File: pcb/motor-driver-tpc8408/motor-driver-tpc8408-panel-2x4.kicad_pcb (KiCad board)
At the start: 2 copper layers, 92 x 90 mm, 202 parts, among them J1 Conn_01x12, U1 TPC8408, U2 TPC8408, U3 74HC00

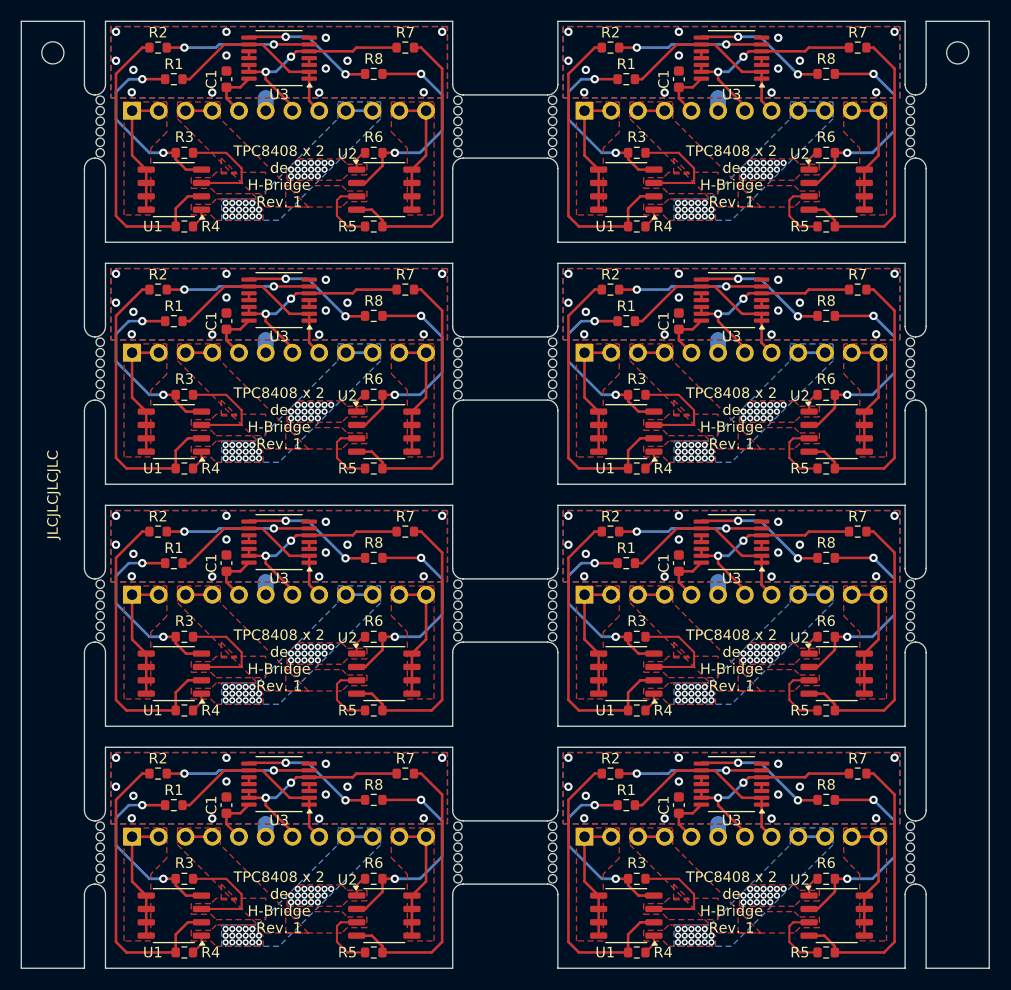
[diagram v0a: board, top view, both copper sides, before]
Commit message: 配線が間違っていたのを修正した
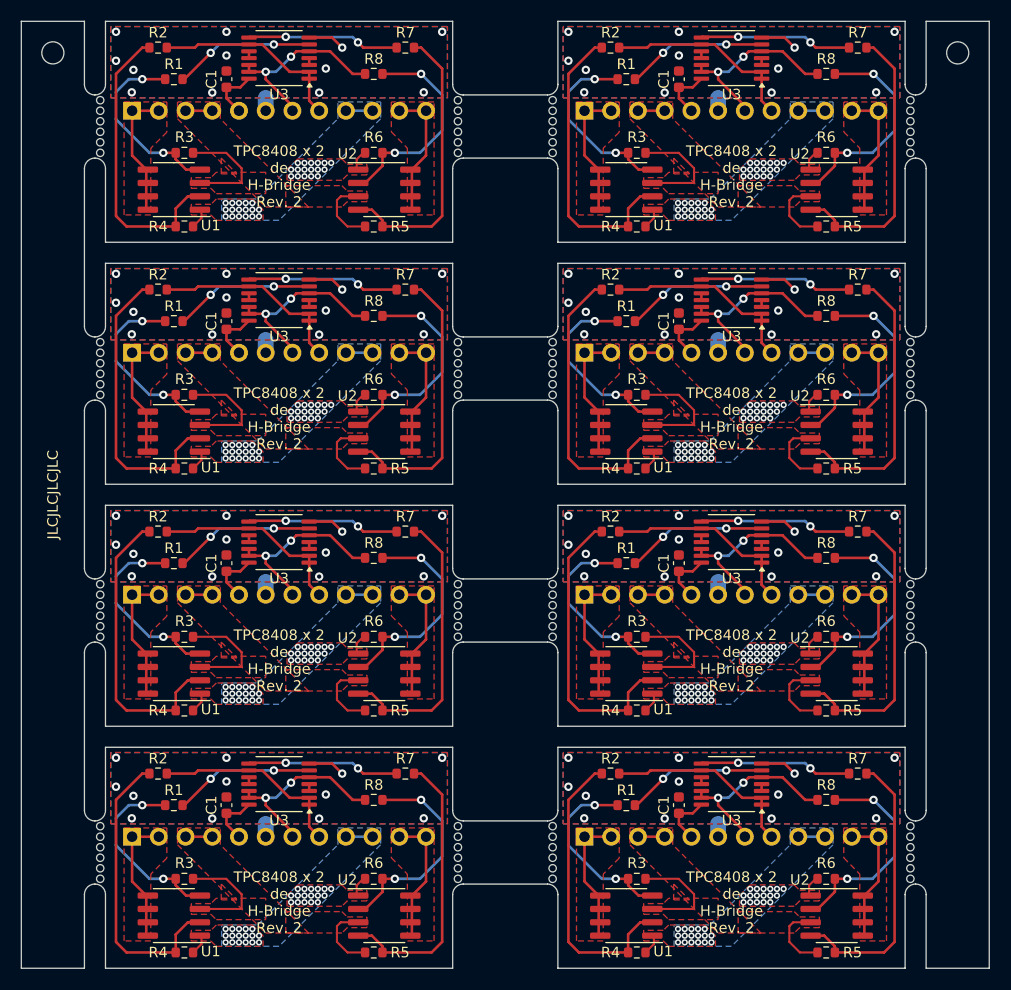
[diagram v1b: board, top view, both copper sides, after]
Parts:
- removed the U1 at (128.0, 115.0)
- removed the U1 at (128.0, 46.0)
- removed the U1 at (128.0, 69.0)
- removed the U1 at (171.0, 69.0)
- removed the U1 at (171.0, 46.0)
- removed the U1 at (171.0, 92.0)
- removed the U1 at (171.0, 115.0)
- removed the U1 at (128.0, 92.0)
- removed the U2 at (191.0, 69.0)
- removed the U2 at (191.0, 115.0)
- removed the U2 at (191.0, 92.0)
- removed the U2 at (148.0, 46.0)
- removed the U2 at (148.0, 115.0)
- removed the U2 at (148.0, 92.0)
- removed the U2 at (148.0, 69.0)
- removed the U2 at (191.0, 46.0)
- added U1: FDS4559, Package_SO:SOIC-8_3.9x4.9mm_P1.27mm, F.Cu at (128.0, 92.0)
- added U1: FDS4559, Package_SO:SOIC-8_3.9x4.9mm_P1.27mm, F.Cu at (171.0, 69.0)
- added U1: FDS4559, Package_SO:SOIC-8_3.9x4.9mm_P1.27mm, F.Cu at (171.0, 46.0)
- added U1: FDS4559, Package_SO:SOIC-8_3.9x4.9mm_P1.27mm, F.Cu at (128.0, 69.0)
- added U1: FDS4559, Package_SO:SOIC-8_3.9x4.9mm_P1.27mm, F.Cu at (128.0, 46.0)
- added U1: FDS4559, Package_SO:SOIC-8_3.9x4.9mm_P1.27mm, F.Cu at (128.0, 115.0)
- added U1: FDS4559, Package_SO:SOIC-8_3.9x4.9mm_P1.27mm, F.Cu at (171.0, 115.0)
- added U1: FDS4559, Package_SO:SOIC-8_3.9x4.9mm_P1.27mm, F.Cu at (171.0, 92.0)
- added U2: FDS4559, Package_SO:SOIC-8_3.9x4.9mm_P1.27mm, F.Cu at (148.0, 69.0)
- added U2: FDS4559, Package_SO:SOIC-8_3.9x4.9mm_P1.27mm, F.Cu at (191.0, 115.0)
- added U2: FDS4559, Package_SO:SOIC-8_3.9x4.9mm_P1.27mm, F.Cu at (148.0, 92.0)
- added U2: FDS4559, Package_SO:SOIC-8_3.9x4.9mm_P1.27mm, F.Cu at (191.0, 92.0)
- added U2: FDS4559, Package_SO:SOIC-8_3.9x4.9mm_P1.27mm, F.Cu at (148.0, 115.0)
- added U2: FDS4559, Package_SO:SOIC-8_3.9x4.9mm_P1.27mm, F.Cu at (148.0, 46.0)
- added U2: FDS4559, Package_SO:SOIC-8_3.9x4.9mm_P1.27mm, F.Cu at (191.0, 69.0)
- added U2: FDS4559, Package_SO:SOIC-8_3.9x4.9mm_P1.27mm, F.Cu at (191.0, 46.0)
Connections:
- R1 pad 2: /IN_B -> /P1 (x8)
- R2 pad 2: /P1 -> /IN_B (x8)
- R7 pad 1: /IN_A -> /P2 (x8)
- R8 pad 1: /P2 -> /IN_A (x8)
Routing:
- net GND: track 9.73 -> 38.0 mm, vias 104 -> 96
- net /IN_A: track 163.1 -> 145.5 mm
- net /P2: track 100.5 -> 115.9 mm
- net /IN_B: track 148.6 -> 150.6 mm
- net /P1: track 109.3 -> 107.2 mm
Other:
- board text added: "@daisuke_ym 2024/09"
- board text added: "TPC8408 x 2 de H-Bridge Rev. 2"
- board text removed: "2024 Aug - @daisuke_ym"
- board text removed: "TPC8408 x 2 de H-Bridge Rev. 1"
